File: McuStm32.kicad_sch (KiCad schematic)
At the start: 1 part, among them U1 STM32F103CBTx

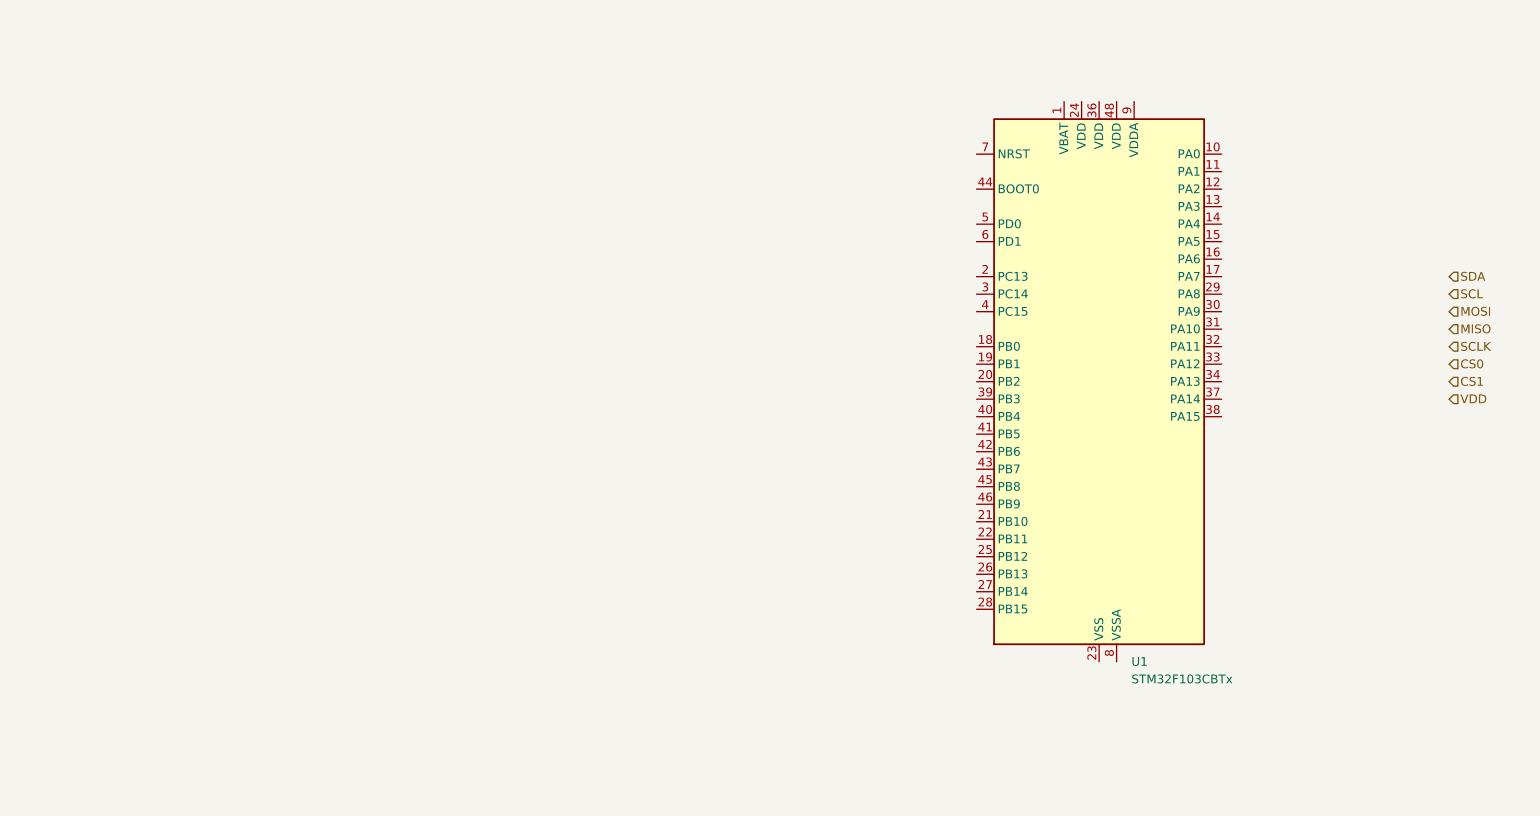
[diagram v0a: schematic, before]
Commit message: Semi finished the regulator-section
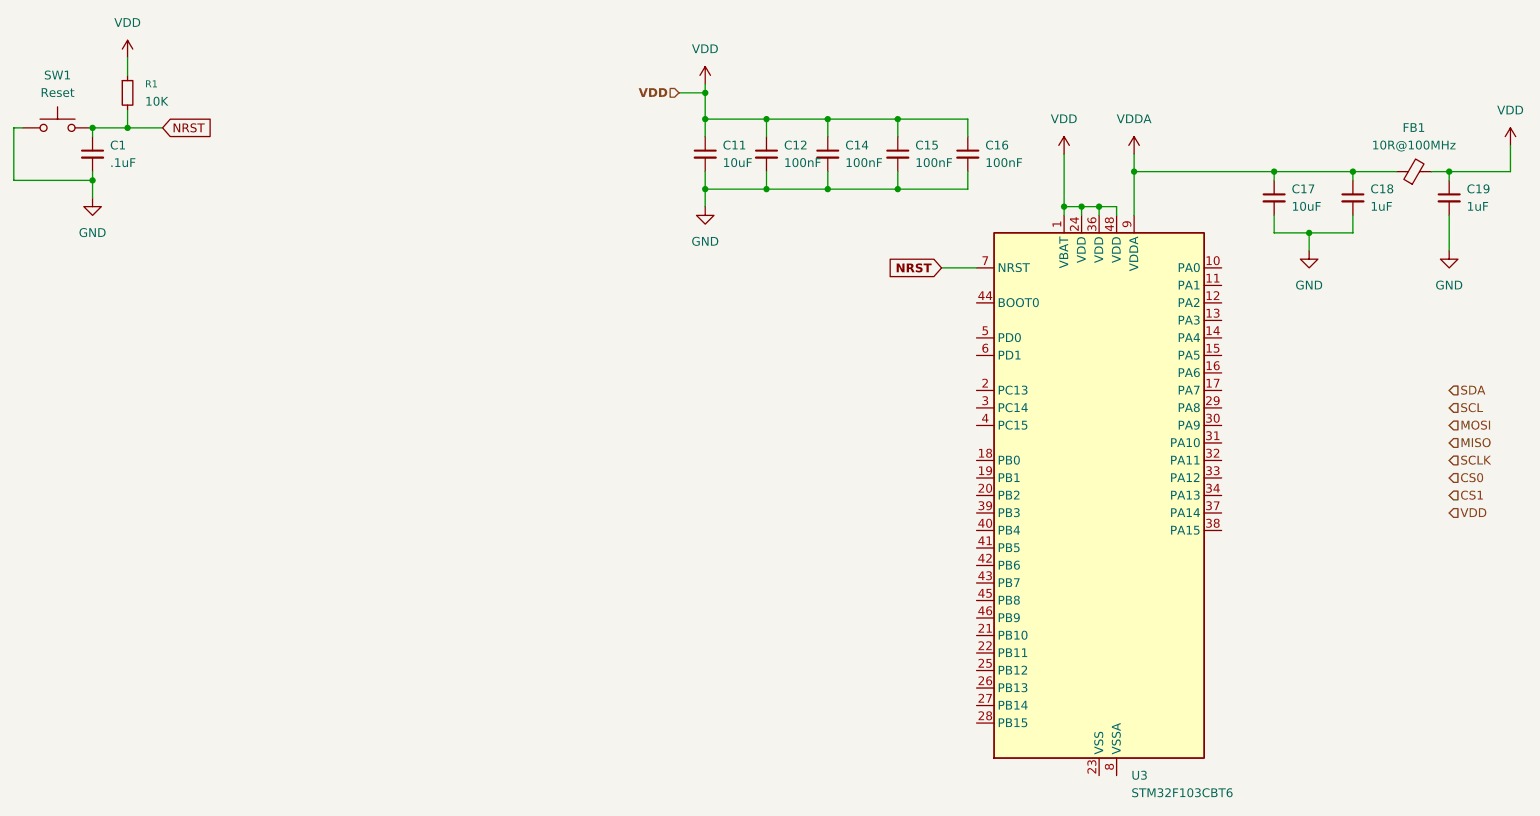
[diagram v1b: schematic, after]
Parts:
- added C1: .1uF, Capacitor_SMD:C_0805_2012Metric, symbol Device:C_Small
- added C11, C17: 10uF, Capacitor_SMD:C_0805_2012Metric, symbol Device:C_Small
- added C12, C14, C15, C16: 100nF, Capacitor_SMD:C_0805_2012Metric, symbol Device:C_Small
- added C18, C19: 1uF, Capacitor_SMD:C_0805_2012Metric, symbol Device:C_Small
- added FB1: 10R@100MHz, Inductor_SMD:L_0201_0603Metric, symbol Device:FerriteBead_Small
- added R1: 10K, Resistor_SMD:R_0805_2012Metric, symbol Device:R_Small
- added SW1: Reset, Button_Switch_SMD:SW_SPST_SKQG_WithStem, symbol Switch:SW_Push
- U3: renamed from U1; value STM32F103CBTx -> STM32F103CBT6
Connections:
- net VDD: now also U3.1 (VBAT), U3.24 (VDD), U3.36 (VDD), U3.48 (VDD), C11.1, C12.1, C14.1, C15.1, C16.1, C19.1, FB1.2, R1.1
- net NRST: now reaches U3.7 (NRST)
- net NRST: now also C1.1, R1.2, SW1.2
- net VDDA: now reaches U3.9 (VDDA)
- net VDDA: now also C17.1, C18.1, FB1.1
- new net GND: C1.2, C11.2, C12.2, C14.2, C15.2, C16.2, C17.2, C18.2, C19.2, SW1.1
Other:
- moved on the sheet: U3
